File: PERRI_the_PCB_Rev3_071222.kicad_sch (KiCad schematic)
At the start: 40 parts, among them J1 SS5-80-3.00-X-D-K-XX, J2 Conn_01x02, J3 Conn_02x50_Counter_Clockwise, J4 Conn_02x05_Counter_Clockwise, J5 SS5-80-3.00-X-D-K-XX, J6 Conn_01x03, J7 Conn_01x03, J8 Conn_01x03, SW2 SW_DIP_x08, U1 TMP441AIDCNR, U2 TPS2595, U3 PCA9554ADB, U4 NCV8508

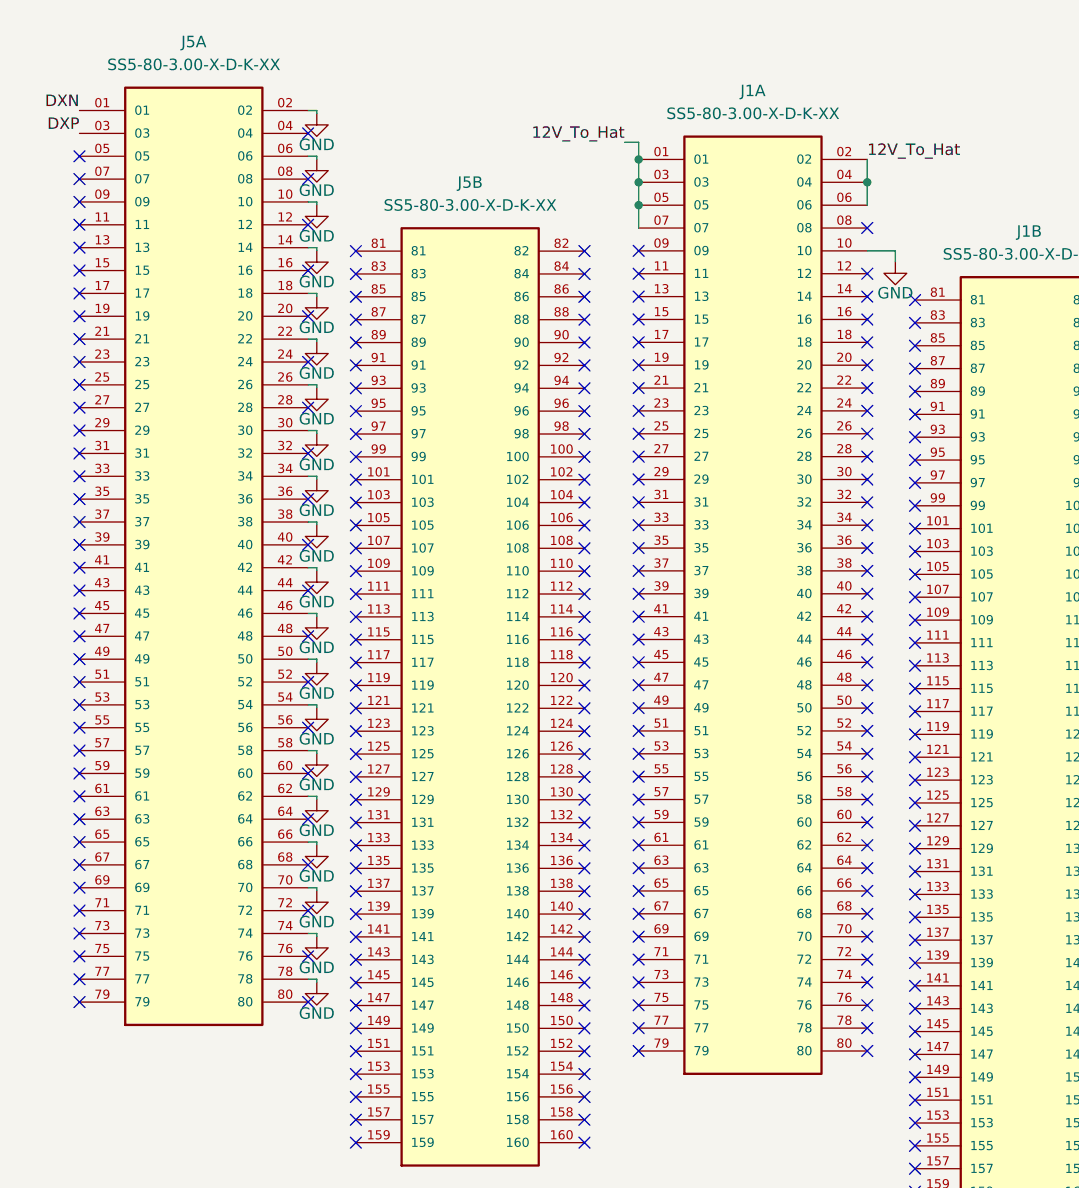
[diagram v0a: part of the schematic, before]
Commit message: Fixed some alignment issues
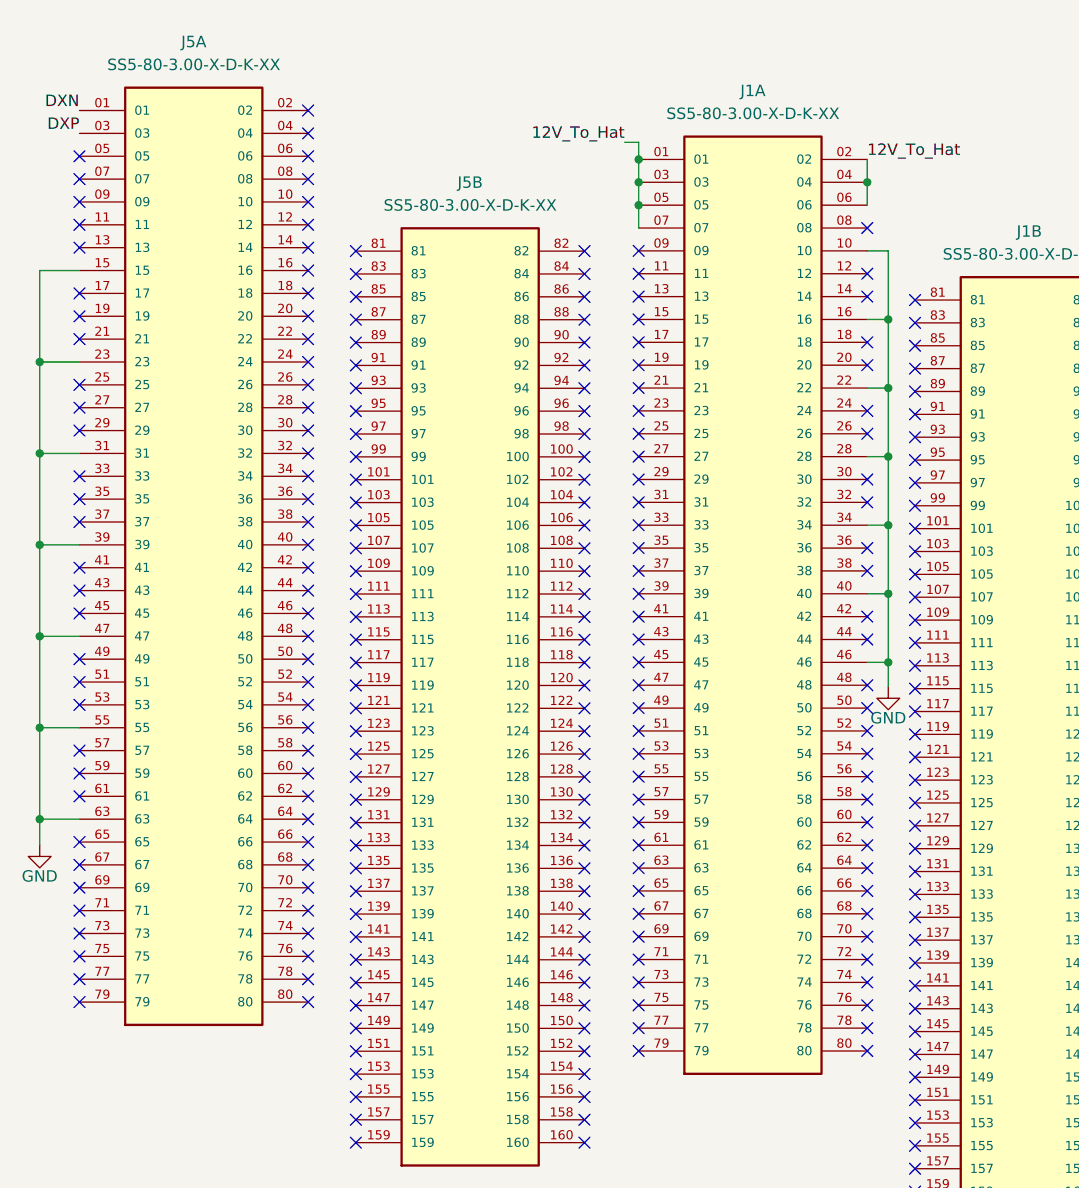
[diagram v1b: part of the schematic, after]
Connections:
- net GND: now also J1.16, J1.22, J1.28, J1.34, J1.40, J1.46, J5.15, J5.23, J5.31, J5.39, J5.47, J5.55, J5.63; no longer J5.02, J5.06, J5.10, J5.14, J5.18, J5.22, J5.26, J5.30, J5.34, J5.38, J5.42, J5.46, J5.50, J5.54, J5.58, J5.62, J5.66, J5.70, J5.74, J5.78
- no-connect marks 376 -> 383
